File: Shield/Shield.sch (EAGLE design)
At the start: 11 parts, among them Q1 NPN, U1 TEMPERATURE-SENSOR

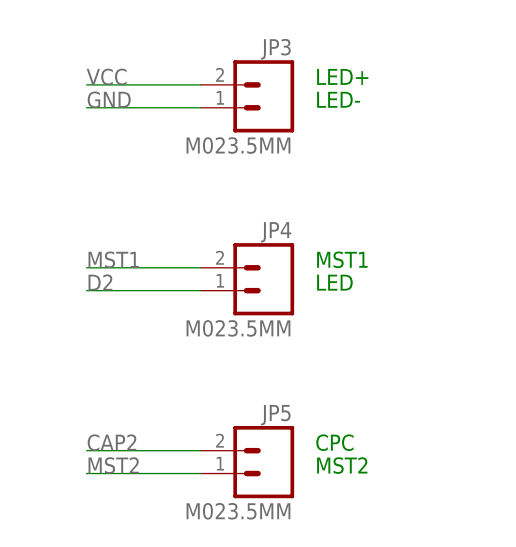
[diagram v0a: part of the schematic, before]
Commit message: fixed D2 pin
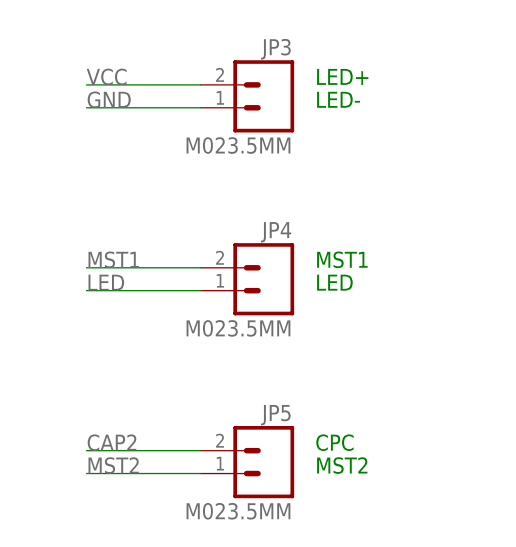
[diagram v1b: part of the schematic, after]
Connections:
- removed net D2: JP4.1
- net LED: now also JP4.1
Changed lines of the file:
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@@
 </busses>
 <nets>
-<net name="D2" class="0">
-<segment>
-<pinref part="JP4" gate="G$1" pin="1"/>
-<wire x1="-33.02" y1="15.24" x2="-45.72" y2="15.24" width="0.1524" layer="91"/>
-<label x="-45.72" y="15.24" size="1.778" layer="95"/>
-</segment>
-</net>
 <net name="MST" class="0">
 <segment>
@@
 <label x="-10.16" y="104.14" size="1.778" layer="95"/>
 </segment>
+<segment>
+<pinref part="JP4" gate="G$1" pin="1"/>
+<wire x1="-33.02" y1="15.24" x2="-45.72" y2="15.24" width="0.1524" layer="91"/>
+<label x="-45.72" y="15.24" size="1.778" layer="95"/>
+</segment>
 </net>

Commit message: finished shield v1.0
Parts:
- YUN1: device SparkFun-Boards:ARDUINO_SHIELDLABEL -> SparkFun-Boards:ARDUINO_SHIELDNO_SILK
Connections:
- net CAP1 renamed CPC1
- net CAP2 renamed CPC2
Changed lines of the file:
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@@
 </classes>
 <parts>
-<part name="YUN1" library="SparkFun-Boards" deviceset="ARDUINO_SHIELD" device="LABEL" value="SHIELD"/>
+<part name="YUN1" library="SparkFun-Boards" deviceset="ARDUINO_SHIELD" device="NO_SILK" value="SHIELD"/>
 <part name="JP2" library="SparkFun-Connectors" deviceset="M02" device="3.5MM"/>
 <part name="JP4" library="SparkFun-Connectors" deviceset="M02" device="3.5MM"/>
@@
 <part name="R7" library="SparkFun-Passives" deviceset="RESISTOR" device="AXIAL-0.3" value="1M"/>
 <part name="U1" library="SparkFun-Sensors" deviceset="TEMPERATURE-SENSOR" device=""/>
+<part name="FRAME1" library="SparkFun-Aesthetics" deviceset="FRAME-A4L" device="">
+<attribute name="CNAME" value="EDEN"/>
+<attribute name="CREVISION" value="1.0"/>
+<attribute name="DESIGNER" value="Joël Gähwiler"/>
+</part>
 </parts>
 <sheets>
@@
 <instance part="R7" gate="G$1" x="40.64" y="22.86"/>
 <instance part="U1" gate="G$1" x="40.64" y="53.34"/>
+<instance part="FRAME1" gate="G$1" x="-93.98" y="-33.02">
+<attribute name="CNAME" x="-93.98" y="-33.02" size="1.778" layer="96" display="off"/>
+<attribute name="CREVISION" x="-93.98" y="-33.02" size="1.778" layer="96" display="off"/>
+<attribute name="DESIGNER" x="-93.98" y="-33.02" size="1.778" layer="96" display="off"/>
+</instance>
 </instances>
 <busses>
@@
 </segment>
 </net>
-<net name="CAP1" class="0">
-<segment>
-<pinref part="YUN1" gate="G$1" pin="*D3"/>
-<wire x1="-17.78" y1="101.6" x2="-5.08" y2="101.6" width="0.1524" layer="91"/>
-<label x="-10.16" y="101.6" size="1.778" layer="95"/>
-</segment>
-<segment>
-<pinref part="R7" gate="G$1" pin="1"/>
-<wire x1="35.56" y1="22.86" x2="20.32" y2="22.86" width="0.1524" layer="91"/>
-<label x="20.32" y="22.86" size="1.778" layer="95"/>
-</segment>
-</net>
-<net name="CAP2" class="0">
-<segment>
-<pinref part="YUN1" gate="G$1" pin="D4"/>
-<wire x1="-17.78" y1="99.06" x2="-5.08" y2="99.06" width="0.1524" layer="91"/>
-<label x="-10.16" y="99.06" size="1.778" layer="95"/>
-</segment>
-<segment>
-<pinref part="R7" gate="G$1" pin="2"/>
-<wire x1="45.72" y1="22.86" x2="60.96" y2="22.86" width="0.1524" layer="91"/>
-<label x="55.88" y="22.86" size="1.778" layer="95"/>
-</segment>
-<segment>
-<pinref part="JP5" gate="G$1" pin="2"/>
-<wire x1="-33.02" y1="-2.54" x2="-45.72" y2="-2.54" width="0.1524" layer="91"/>
-<label x="-45.72" y="-2.54" size="1.778" layer="95"/>
-</segment>
-</net>
 <net name="GND" class="0">
 <segment>
@@
 </segment>
 </net>
+<net name="CPC1" class="0">
+<segment>
+<pinref part="YUN1" gate="G$1" pin="*D3"/>
+<wire x1="-17.78" y1="101.6" x2="-5.08" y2="101.6" width="0.1524" layer="91"/>
+<label x="-10.16" y="101.6" size="1.778" layer="95"/>
+</segment>
+<segment>
+<pinref part="R7" gate="G$1" pin="1"/>
+<wire x1="35.56" y1="22.86" x2="20.32" y2="22.86" width="0.1524" layer="91"/>
+<label x="20.32" y="22.86" size="1.778" layer="95"/>
+</segment>
+</net>
+<net name="CPC2" class="0">
+<segment>
+<pinref part="YUN1" gate="G$1" pin="D4"/>
+<wire x1="-17.78" y1="99.06" x2="-5.08" y2="99.06" width="0.1524" layer="91"/>
+<label x="-10.16" y="99.06" size="1.778" layer="95"/>
+</segment>
+<segment>
+<pinref part="JP5" gate="G$1" pin="2"/>
+<wire x1="-33.02" y1="-2.54" x2="-45.72" y2="-2.54" width="0.1524" layer="91"/>
+<label x="-45.72" y="-2.54" size="1.778" layer="95"/>
+</segment>
+<segment>
+<pinref part="R7" gate="G$1" pin="2"/>
+<wire x1="45.72" y1="22.86" x2="60.96" y2="22.86" width="0.1524" layer="91"/>
+<label x="55.88" y="22.86" size="1.778" layer="95"/>
+</segment>
+</net>

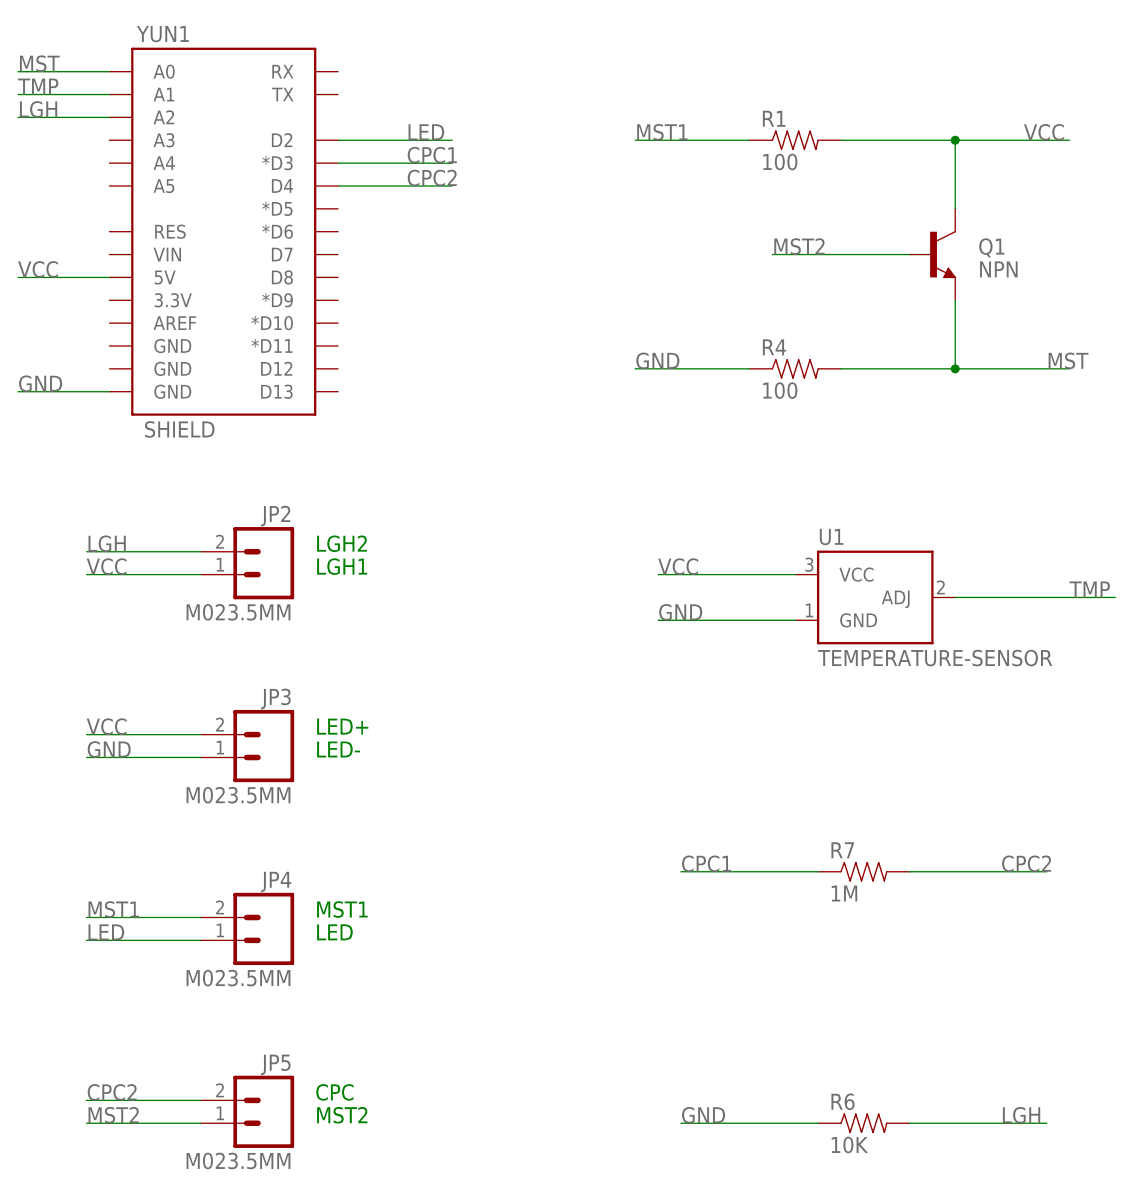
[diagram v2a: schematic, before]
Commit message: added capacitor to temperature circuit
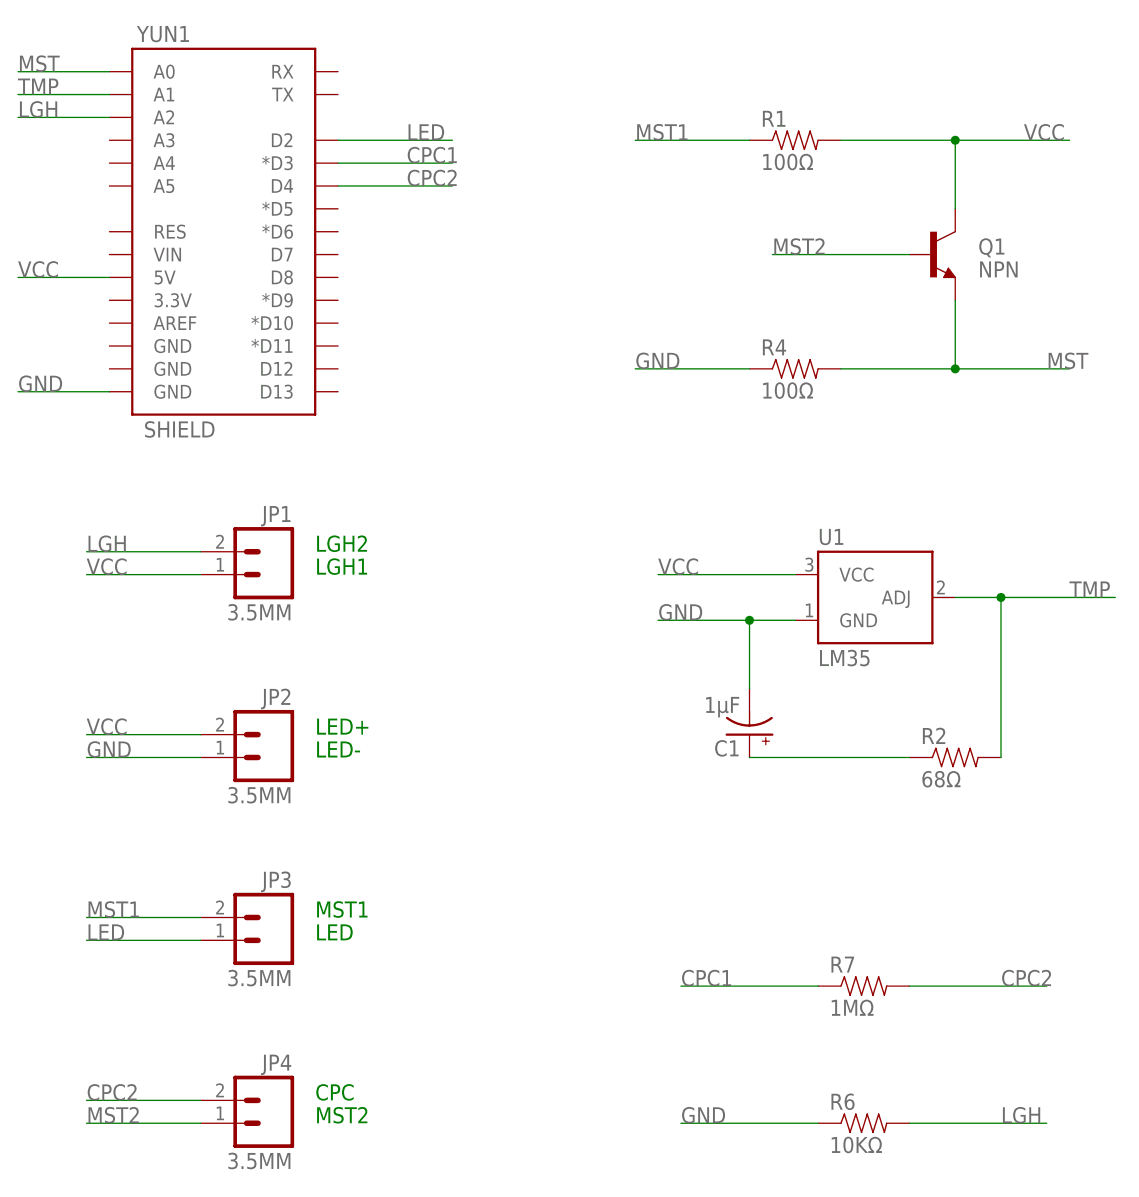
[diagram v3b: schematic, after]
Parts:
- removed JP5: M023.5MM, SparkFun-Connectors:M023.5MM
- added C1: 1µF, SparkFun-Capacitors:CAP_POLPTH1
- added JP1: 3.5MM, SparkFun-Connectors:M023.5MM
- added R2: 68Ω, SparkFun-Passives:RESISTORAXIAL-0.3
- JP2, JP3, JP4: value M023.5MM -> 3.5MM
- R1, R4: value 100 -> 100Ω
- R6: value 10K -> 10KΩ
- R7: value 1M -> 1MΩ
- U1: value TEMPERATURE-SENSOR -> LM35
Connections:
- new net N$1: C1.+, R2.1
- net CPC2: now also JP4.2; no longer JP5.2
- net GND: now also C1.-, JP2.1; no longer JP3.1
- net LED: now also JP3.1; no longer JP4.1
- net LGH: now also JP1.2; no longer JP2.2
- net MST1: now also JP3.2; no longer JP4.2
- net MST2: now also JP4.1; no longer JP5.1
- net TMP: now also R2.2
- net VCC: now also JP1.1, JP2.2; no longer JP2.1, JP3.2
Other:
- moved on the sheet: JP2, JP3, JP4, R7
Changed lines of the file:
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@@
 <parts>
 <part name="YUN1" library="SparkFun-Boards" deviceset="ARDUINO_SHIELD" device="NO_SILK" value="SHIELD"/>
-<part name="JP2" library="SparkFun-Connectors" deviceset="M02" device="3.5MM"/>
-<part name="JP4" library="SparkFun-Connectors" deviceset="M02" device="3.5MM"/>
-<part name="JP5" library="SparkFun-Connectors" deviceset="M02" device="3.5MM"/>
-<part name="JP3" library="SparkFun-Connectors" deviceset="M02" device="3.5MM"/>
+<part name="JP1" library="SparkFun-Connectors" deviceset="M02" device="3.5MM" value="3.5MM"/>
+<part name="JP3" library="SparkFun-Connectors" deviceset="M02" device="3.5MM" value="3.5MM"/>
+<part name="JP4" library="SparkFun-Connectors" deviceset="M02" device="3.5MM" value="3.5MM"/>
+<part name="JP2" library="SparkFun-Connectors" deviceset="M02" device="3.5MM" value="3.5MM"/>
 <part name="Q1" library="SparkFun-DiscreteSemi" deviceset="TRANSISTOR_NPN" device="BC547" value="NPN"/>
-<part name="R1" library="SparkFun-Passives" deviceset="RESISTOR" device="AXIAL-0.3" value="100"/>
-<part name="R4" library="SparkFun-Passives" deviceset="RESISTOR" device="AXIAL-0.3" value="100"/>
-<part name="R6" library="SparkFun-Passives" deviceset="RESISTOR" device="AXIAL-0.3" value="10K"/>
-<part name="R7" library="SparkFun-Passives" deviceset="RESISTOR" device="AXIAL-0.3" value="1M"/>
-<part name="U1" library="SparkFun-Sensors" deviceset="TEMPERATURE-SENSOR" device=""/>
+<part name="R1" library="SparkFun-Passives" deviceset="RESISTOR" device="AXIAL-0.3" value="100Ω"/>
+<part name="R4" library="SparkFun-Passives" deviceset="RESISTOR" device="AXIAL-0.3" value="100Ω"/>
+<part name="R6" library="SparkFun-Passives" deviceset="RESISTOR" device="AXIAL-0.3" value="10KΩ"/>
+<part name="R7" library="SparkFun-Passives" deviceset="RESISTOR" device="AXIAL-0.3" value="1MΩ"/>
+<part name="U1" library="SparkFun-Sensors" deviceset="TEMPERATURE-SENSOR" device="" value="LM35"/>
 <part name="FRAME1" library="SparkFun-Aesthetics" deviceset="FRAME-A4L" device="">
 <attribute name="CNAME" value="EDEN"/>
@@
 <attribute name="DESIGNER" value="Joël Gähwiler"/>
 </part>
+<part name="C1" library="SparkFun-Capacitors" deviceset="CAP_POL" device="PTH1" value="1µF"/>
+<part name="R2" library="SparkFun-Passives" deviceset="RESISTOR" device="AXIAL-0.3" value="68Ω"/>
 </parts>
 <sheets>
@@
 <instances>
 <instance part="YUN1" gate="G$1" x="-30.48" y="93.98"/>
-<instance part="JP2" gate="G$1" x="-25.4" y="55.88" rot="MR0"/>
-<instance part="JP4" gate="G$1" x="-25.4" y="15.24" rot="MR0"/>
-<instance part="JP5" gate="G$1" x="-25.4" y="-5.08" rot="MR0"/>
-<instance part="JP3" gate="G$1" x="-25.4" y="35.56" rot="MR0"/>
+<instance part="JP1" gate="G$1" x="-25.4" y="55.88" rot="MR0"/>
+<instance part="JP3" gate="G$1" x="-25.4" y="15.24" rot="MR0"/>
+<instance part="JP4" gate="G$1" x="-25.4" y="-5.08" rot="MR0"/>
+<instance part="JP2" gate="G$1" x="-25.4" y="35.56" rot="MR0"/>
 <instance part="Q1" gate="G$1" x="48.26" y="91.44"/>
 <instance part="R1" gate="G$1" x="33.02" y="104.14" smashed="yes">
@@
 <instance part="R4" gate="G$1" x="33.02" y="78.74"/>
 <instance part="R6" gate="G$1" x="40.64" y="-5.08"/>
-<instance part="R7" gate="G$1" x="40.64" y="22.86"/>
+<instance part="R7" gate="G$1" x="40.64" y="10.16"/>
 <instance part="U1" gate="G$1" x="40.64" y="53.34"/>
 <instance part="FRAME1" gate="G$1" x="-93.98" y="-33.02">
@@
 <attribute name="DESIGNER" x="-93.98" y="-33.02" size="1.778" layer="96" display="off"/>
 </instance>
+<instance part="C1" gate="G$1" x="27.94" y="38.1" rot="R180"/>
+<instance part="R2" gate="G$1" x="50.8" y="35.56"/>
 </instances>
 <busses>
@@
 <segment>
 <pinref part="U1" gate="G$1" pin="ADJ"/>
-<wire x1="50.8" y1="53.34" x2="68.58" y2="53.34" width="0.1524" layer="91"/>
+<wire x1="50.8" y1="53.34" x2="55.88" y2="53.34" width="0.1524" layer="91"/>
 <label x="63.5" y="53.34" size="1.778" layer="95"/>
+<pinref part="R2" gate="G$1" pin="2"/>
+<wire x1="55.88" y1="53.34" x2="68.58" y2="53.34" width="0.1524" layer="91"/>
+<wire x1="55.88" y1="35.56" x2="55.88" y2="53.34" width="0.1524" layer="91"/>
+<junction x="55.88" y="53.34"/>
 </segment>
 </net>
@@
 </segment>
 <segment>
-<pinref part="JP2" gate="G$1" pin="2"/>
+<pinref part="JP1" gate="G$1" pin="2"/>
 <wire x1="-33.02" y1="58.42" x2="-45.72" y2="58.42" width="0.1524" layer="91"/>
 <label x="-45.72" y="58.42" size="1.778" layer="95"/>
@@
 </segment>
 <segment>
-<pinref part="JP3" gate="G$1" pin="1"/>
+<pinref part="JP2" gate="G$1" pin="1"/>
 <wire x1="-45.72" y1="35.56" x2="-33.02" y2="35.56" width="0.1524" layer="91"/>
 <label x="-45.72" y="35.56" size="1.778" layer="95"/>
@@
 <segment>
 <pinref part="U1" gate="G$1" pin="GND"/>
-<wire x1="33.02" y1="50.8" x2="17.78" y2="50.8" width="0.1524" layer="91"/>
+<wire x1="33.02" y1="50.8" x2="27.94" y2="50.8" width="0.1524" layer="91"/>
 <label x="17.78" y="50.8" size="1.778" layer="95"/>
+<pinref part="C1" gate="G$1" pin="-"/>
+<wire x1="27.94" y1="50.8" x2="17.78" y2="50.8" width="0.1524" layer="91"/>
+<wire x1="27.94" y1="43.18" x2="27.94" y2="50.8" width="0.1524" layer="91"/>
+<junction x="27.94" y="50.8"/>
 </segment>
 <segment>
@@
 </segment>
 <segment>
-<pinref part="JP3" gate="G$1" pin="2"/>
+<pinref part="JP2" gate="G$1" pin="2"/>
 <wire x1="-45.72" y1="38.1" x2="-33.02" y2="38.1" width="0.1524" layer="91"/>
 <label x="-45.72" y="38.1" size="1.778" layer="95"/>
@@
 </segment>
 <segment>
-<pinref part="JP2" gate="G$1" pin="1"/>
+<pinref part="JP1" gate="G$1" pin="1"/>
 <wire x1="-33.02" y1="55.88" x2="-45.72" y2="55.88" width="0.1524" layer="91"/>
 <label x="-45.72" y="55.88" size="1.778" layer="95"/>
@@
 <net name="MST1" class="0">
 <segment>
-<pinref part="JP4" gate="G$1" pin="2"/>
+<pinref part="JP3" gate="G$1" pin="2"/>
 <wire x1="-33.02" y1="17.78" x2="-45.72" y2="17.78" width="0.1524" layer="91"/>
 <label x="-45.72" y="17.78" size="1.778" layer="95"/>
@@
 <net name="MST2" class="0">
 <segment>
-<pinref part="JP5" gate="G$1" pin="1"/>
+<pinref part="JP4" gate="G$1" pin="1"/>
 <wire x1="-33.02" y1="-5.08" x2="-45.72" y2="-5.08" width="0.1524" layer="91"/>
 <label x="-45.72" y="-5.08" size="1.778" layer="95"/>
@@
 </segment>
 <segment>
-<pinref part="JP4" gate="G$1" pin="1"/>
+<pinref part="JP3" gate="G$1" pin="1"/>
 <wire x1="-33.02" y1="15.24" x2="-45.72" y2="15.24" width="0.1524" layer="91"/>
 <label x="-45.72" y="15.24" size="1.778" layer="95"/>
@@
 <segment>
 <pinref part="R7" gate="G$1" pin="1"/>
-<wire x1="35.56" y1="22.86" x2="20.32" y2="22.86" width="0.1524" layer="91"/>
-<label x="20.32" y="22.86" size="1.778" layer="95"/>
+<wire x1="35.56" y1="10.16" x2="20.32" y2="10.16" width="0.1524" layer="91"/>
+<label x="20.32" y="10.16" size="1.778" layer="95"/>
 </segment>
 </net>
@@
 </segment>
 <segment>
-<pinref part="JP5" gate="G$1" pin="2"/>
+<pinref part="JP4" gate="G$1" pin="2"/>
 <wire x1="-33.02" y1="-2.54" x2="-45.72" y2="-2.54" width="0.1524" layer="91"/>
 <label x="-45.72" y="-2.54" size="1.778" layer="95"/>
@@
 <segment>
 <pinref part="R7" gate="G$1" pin="2"/>
-<wire x1="45.72" y1="22.86" x2="60.96" y2="22.86" width="0.1524" layer="91"/>
-<label x="55.88" y="22.86" size="1.778" layer="95"/>
-</segment>
-</net>
+<wire x1="45.72" y1="10.16" x2="60.96" y2="10.16" width="0.1524" layer="91"/>
+<label x="55.88" y="10.16" size="1.778" layer="95"/>
+</segment>
+</net>
+<net name="N$1" class="0">
+<segment>
+<pinref part="R2" gate="G$1" pin="1"/>
+<pinref part="C1" gate="G$1" pin="+"/>
+<wire x1="45.72" y1="35.56" x2="27.94" y2="35.56" width="0.1524" layer="91"/>
+</segment>
+</net>
